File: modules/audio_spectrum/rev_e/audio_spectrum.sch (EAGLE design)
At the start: 109 parts, among them J1 AUDIO-JACK-VERTICAL, J2 MODULE_GENERIC_DEBUG, J3 TC2030-JLINK-L, P1 4k-200k, P2 4k-200k, Q1 NX3008PBK, Q2 NX3008PBK, U1 AT45DB641EUDFN, U10 TLV62130, U2 MP23AB02B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

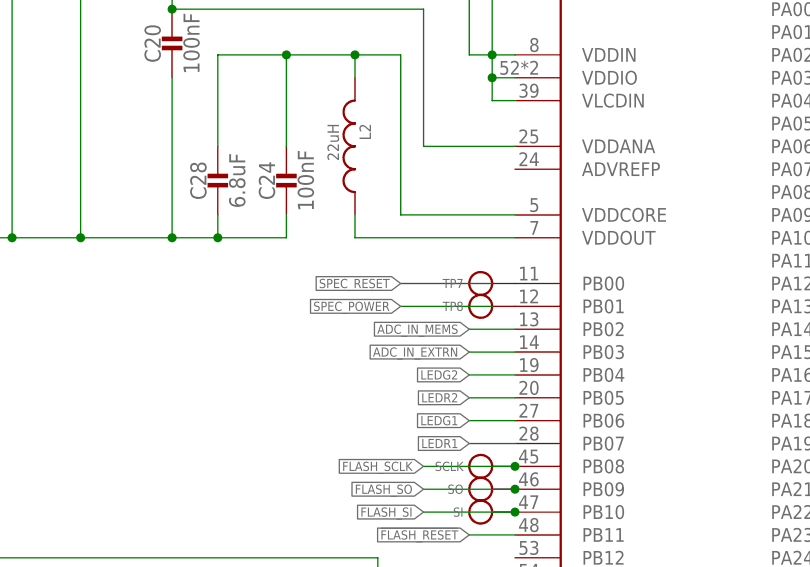
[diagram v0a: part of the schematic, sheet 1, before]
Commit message: fixed spec reset airwire
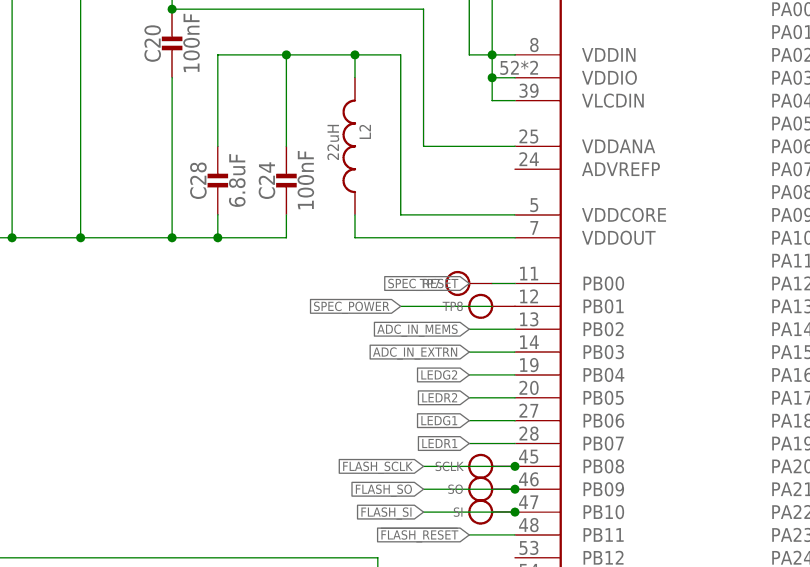
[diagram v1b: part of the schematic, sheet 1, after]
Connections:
- removed net N$22: TP7.TESTPOINT, U9.PB00
- net SPEC_RESET: now also TP7.TESTPOINT, U9.PB00
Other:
- moved on the sheet: TP7
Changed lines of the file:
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@@
 <grid distance="0.1" unitdist="inch" unit="inch" style="lines" multiple="1" display="yes" altdistance="0.05" altunitdist="inch" altunit="inch"/>
 <layers>
-<layer number="1" name="Top" color="4" fill="1" visible="yes" active="no"/>
-<layer number="2" name="Route2" color="1" fill="3" visible="yes" active="no"/>
-<layer number="3" name="Route3" color="4" fill="3" visible="yes" active="no"/>
-<layer number="4" name="Route4" color="1" fill="4" visible="yes" active="no"/>
-<layer number="5" name="Route5" color="4" fill="4" visible="yes" active="no"/>
-<layer number="6" name="Route6" color="1" fill="8" visible="yes" active="no"/>
-<layer number="7" name="Route7" color="4" fill="8" visible="yes" active="no"/>
-<layer number="8" name="Route8" color="1" fill="2" visible="yes" active="no"/>
-<layer number="9" name="Route9" color="4" fill="2" visible="yes" active="no"/>
-<layer number="10" name="Route10" color="1" fill="7" visible="yes" active="no"/>
-<layer number="11" name="Route11" color="4" fill="7" visible="yes" active="no"/>
-<layer number="12" name="Route12" color="1" fill="5" visible="yes" active="no"/>
-<layer number="13" name="Route13" color="4" fill="5" visible="yes" active="no"/>
-<layer number="14" name="Route14" color="1" fill="6" visible="yes" active="no"/>
-<layer number="15" name="Route15" color="4" fill="6" visible="yes" active="no"/>
-<layer number="16" name="Bottom" color="1" fill="1" visible="yes" active="no"/>
-<layer number="17" name="Pads" color="2" fill="1" visible="yes" active="no"/>
-<layer number="18" name="Vias" color="2" fill="1" visible="yes" active="no"/>
-<layer number="19" name="Unrouted" color="6" fill="1" visible="yes" active="no"/>
-<layer number="20" name="Dimension" color="15" fill="1" visible="yes" active="no"/>
-<layer number="21" name="tPlace" color="7" fill="1" visible="yes" active="no"/>
-<layer number="22" name="bPlace" color="7" fill="1" visible="yes" active="no"/>
-<layer number="23" name="tOrigins" color="15" fill="1" visible="yes" active="no"/>
-<layer number="24" name="bOrigins" color="15" fill="1" visible="yes" active="no"/>
-<layer number="25" name="tNames" color="7" fill="1" visible="yes" active="no"/>
-<layer number="26" name="bNames" color="7" fill="1" visible="yes" active="no"/>
-<layer number="27" name="tValues" color="7" fill="1" visible="yes" active="no"/>
-<layer number="28" name="bValues" color="7" fill="1" visible="yes" active="no"/>
+<layer number="1" name="Top" color="4" fill="1" visible="no" active="no"/>
+<layer number="2" name="Route2" color="1" fill="3" visible="no" active="no"/>
+<layer number="3" name="Route3" color="4" fill="3" visible="no" active="no"/>
+<layer number="4" name="Route4" color="1" fill="4" visible="no" active="no"/>
+<layer number="5" name="Route5" color="4" fill="4" visible="no" active="no"/>
+<layer number="6" name="Route6" color="1" fill="8" visible="no" active="no"/>
+<layer number="7" name="Route7" color="4" fill="8" visible="no" active="no"/>
+<layer number="8" name="Route8" color="1" fill="2" visible="no" active="no"/>
+<layer number="9" name="Route9" color="4" fill="2" visible="no" active="no"/>
+<layer number="10" name="Route10" color="1" fill="7" visible="no" active="no"/>
+<layer number="11" name="Route11" color="4" fill="7" visible="no" active="no"/>
+<layer number="12" name="Route12" color="1" fill="5" visible="no" active="no"/>
+<layer number="13" name="Route13" color="4" fill="5" visible="no" active="no"/>
+<layer number="14" name="Route14" color="1" fill="6" visible="no" active="no"/>
+<layer number="15" name="Route15" color="4" fill="6" visible="no" active="no"/>
+<layer number="16" name="Bottom" color="1" fill="1" visible="no" active="no"/>
+<layer number="17" name="Pads" color="2" fill="1" visible="no" active="no"/>
+<layer number="18" name="Vias" color="2" fill="1" visible="no" active="no"/>
+<layer number="19" name="Unrouted" color="6" fill="1" visible="no" active="no"/>
+<layer number="20" name="Dimension" color="15" fill="1" visible="no" active="no"/>
+<layer number="21" name="tPlace" color="7" fill="1" visible="no" active="no"/>
+<layer number="22" name="bPlace" color="7" fill="1" visible="no" active="no"/>
+<layer number="23" name="tOrigins" color="15" fill="1" visible="no" active="no"/>
+<layer number="24" name="bOrigins" color="15" fill="1" visible="no" active="no"/>
+<layer number="25" name="tNames" color="7" fill="1" visible="no" active="no"/>
+<layer number="26" name="bNames" color="7" fill="1" visible="no" active="no"/>
+<layer number="27" name="tValues" color="7" fill="1" visible="no" active="no"/>
+<layer number="28" name="bValues" color="7" fill="1" visible="no" active="no"/>
 <layer number="29" name="tStop" color="7" fill="3" visible="no" active="no"/>
 <layer number="30" name="bStop" color="7" fill="6" visible="no" active="no"/>
@@
 <layer number="35" name="tGlue" color="7" fill="4" visible="no" active="no"/>
 <layer number="36" name="bGlue" color="7" fill="5" visible="no" active="no"/>
-<layer number="37" name="tTest" color="7" fill="1" visible="yes" active="no"/>
-<layer number="38" name="bTest" color="7" fill="1" visible="yes" active="no"/>
+<layer number="37" name="tTest" color="7" fill="1" visible="no" active="no"/>
+<layer number="38" name="bTest" color="7" fill="1" visible="no" active="no"/>
 <layer number="39" name="tKeepout" color="4" fill="11" visible="no" active="no"/>
 <layer number="40" name="bKeepout" color="1" fill="11" visible="no" active="no"/>
@@
 <layer number="44" name="Drills" color="7" fill="1" visible="no" active="no"/>
 <layer number="45" name="Holes" color="7" fill="1" visible="no" active="no"/>
-<layer number="46" name="Milling" color="3" fill="1" visible="yes" active="no"/>
-<layer number="47" name="Measures" color="7" fill="1" visible="yes" active="no"/>
-<layer number="48" name="Document" color="7" fill="1" visible="yes" active="no"/>
-<layer number="49" name="Reference" color="7" fill="1" visible="yes" active="no"/>
-<layer number="50" name="dxf" color="7" fill="1" visible="yes" active="no"/>
-<layer number="51" name="tDocu" color="7" fill="1" visible="yes" active="no"/>
-<layer number="52" name="bDocu" color="7" fill="1" visible="yes" active="no"/>
-<layer number="53" name="tGND_GNDA" color="7" fill="9" visible="yes" active="no"/>
-<layer number="54" name="bGND_GNDA" color="1" fill="9" visible="yes" active="no"/>
-<layer number="56" name="wert" color="7" fill="1" visible="yes" active="no"/>
-<layer number="57" name="tCAD" color="7" fill="1" visible="yes" active="no"/>
-<layer number="59" name="Invisible" color="7" fill="1" visible="yes" active="no"/>
-<layer number="60" name="bCarbon" color="7" fill="1" visible="yes" active="no"/>
-<layer number="61" name="stand" color="7" fill="1" visible="yes" active="no"/>
+<layer number="46" name="Milling" color="3" fill="1" visible="no" active="no"/>
+<layer number="47" name="Measures" color="7" fill="1" visible="no" active="no"/>
+<layer number="48" name="Document" color="7" fill="1" visible="no" active="no"/>
+<layer number="49" name="Reference" color="7" fill="1" visible="no" active="no"/>
+<layer number="50" name="dxf" color="7" fill="1" visible="no" active="no"/>
+<layer number="51" name="tDocu" color="7" fill="1" visible="no" active="no"/>
+<layer number="52" name="bDocu" color="7" fill="1" visible="no" active="no"/>
+<layer number="53" name="tGND_GNDA" color="7" fill="9" visible="no" active="no"/>
+<layer number="54" name="bGND_GNDA" color="1" fill="9" visible="no" active="no"/>
+<layer number="56" name="wert" color="7" fill="1" visible="no" active="no"/>
+<layer number="57" name="tCAD" color="7" fill="1" visible="no" active="no"/>
+<layer number="59" name="Invisible" color="7" fill="1" visible="no" active="no"/>
+<layer number="60" name="bCarbon" color="7" fill="1" visible="no" active="no"/>
+<layer number="61" name="stand" color="7" fill="1" visible="no" active="no"/>
 <layer number="90" name="Modules" color="5" fill="1" visible="no" active="no"/>
 <layer number="91" name="Nets" color="2" fill="1" visible="yes" active="yes"/>
@@
 <instance part="TP5" gate="G$1" x="175.26" y="142.24" rot="R180"/>
 <instance part="TP6" gate="G$1" x="175.26" y="132.08" rot="R180"/>
-<instance part="TP7" gate="G$1" x="127" y="127"/>
+<instance part="TP7" gate="G$1" x="124.46" y="127"/>
 <instance part="TP8" gate="G$1" x="127" y="124.46"/>
 <instance part="GND16" gate="1" x="210.82" y="25.4"/>
@@
 </segment>
 </net>
-<net name="N$22" class="0">
+<net name="SPEC_RESET" class="0">
 <segment>
 <pinref part="TP7" gate="G$1" pin="TESTPOINT"/>
 <pinref part="U9" gate="U1" pin="PB00"/>
-</segment>
-</net>
-<net name="SPEC_RESET" class="0">
-<segment>
-<wire x1="127" y1="127" x2="116.84" y2="127" width="0.1524" layer="91"/>
-<label x="116.84" y="127" size="1.016" layer="95" rot="R180" xref="yes"/>
-</segment>
-</net>
+<wire x1="127" y1="127" x2="129.54" y2="127" width="0.1524" layer="91"/>
+<label x="124.46" y="127" size="1.016" layer="95" rot="R180" xref="yes"/>
+</segment>
+</net>
